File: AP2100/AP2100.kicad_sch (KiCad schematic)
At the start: 0 parts

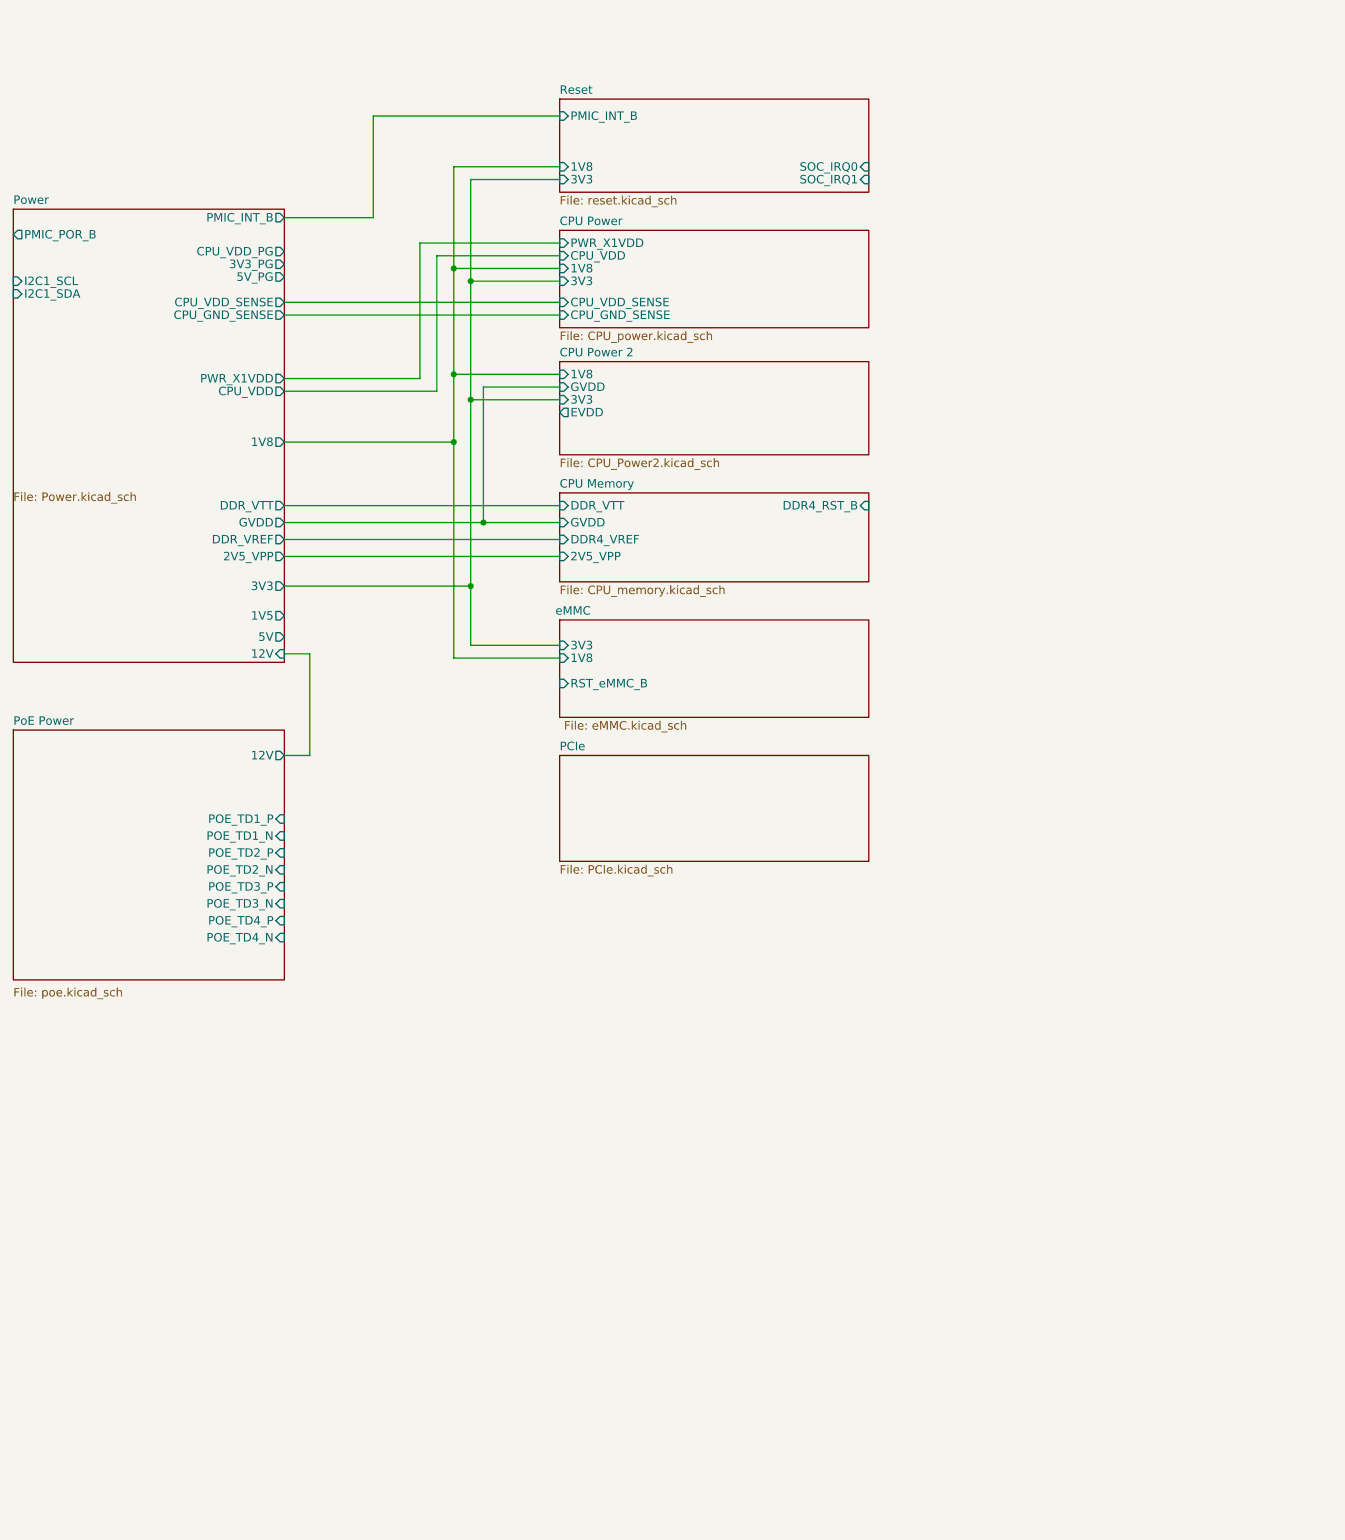
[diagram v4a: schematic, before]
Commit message: Add clocking and start of ethernet
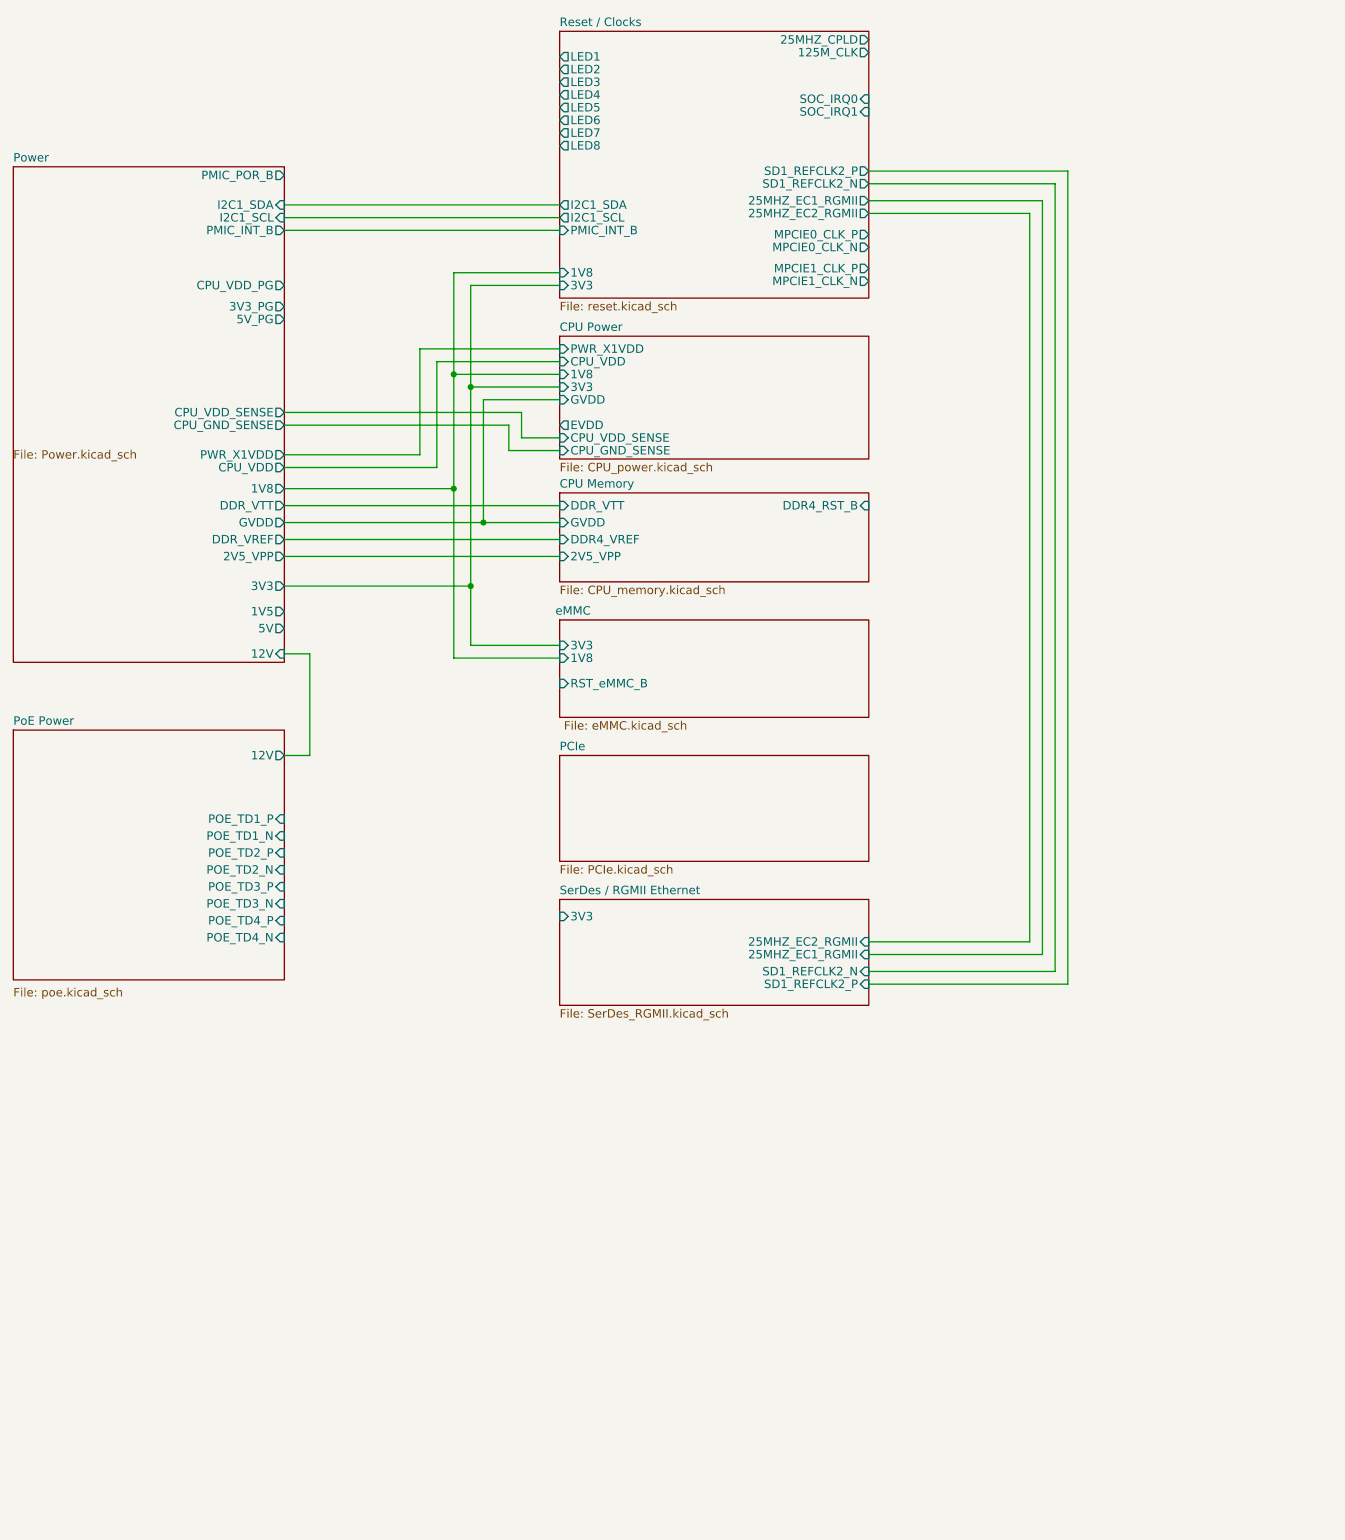
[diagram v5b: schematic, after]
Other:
- sheet Reset renamed Reset / Clocks
- removed sheet CPU Power 2
- added sheet SerDes / RGMII Ethernet (SerDes_RGMII.kicad_sch)
- sheet CPU Power ports: added EVDD, GVDD; removed none
- sheet Reset / Clocks ports: added 125M_CLK, 25MHZ_CPLD, 25MHZ_EC1_RGMII, 25MHZ_EC2_RGMII, I2C1_SCL, I2C1_SDA, LED1, LED2, LED3, LED4, LED5, LED6, LED7, LED8, MPCIE0_CLK_N, MPCIE0_CLK_P, MPCIE1_CLK_N, MPCIE1_CLK_P, SD1_REFCLK2_N, SD1_REFCLK2_P; removed none

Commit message: Finish reset section
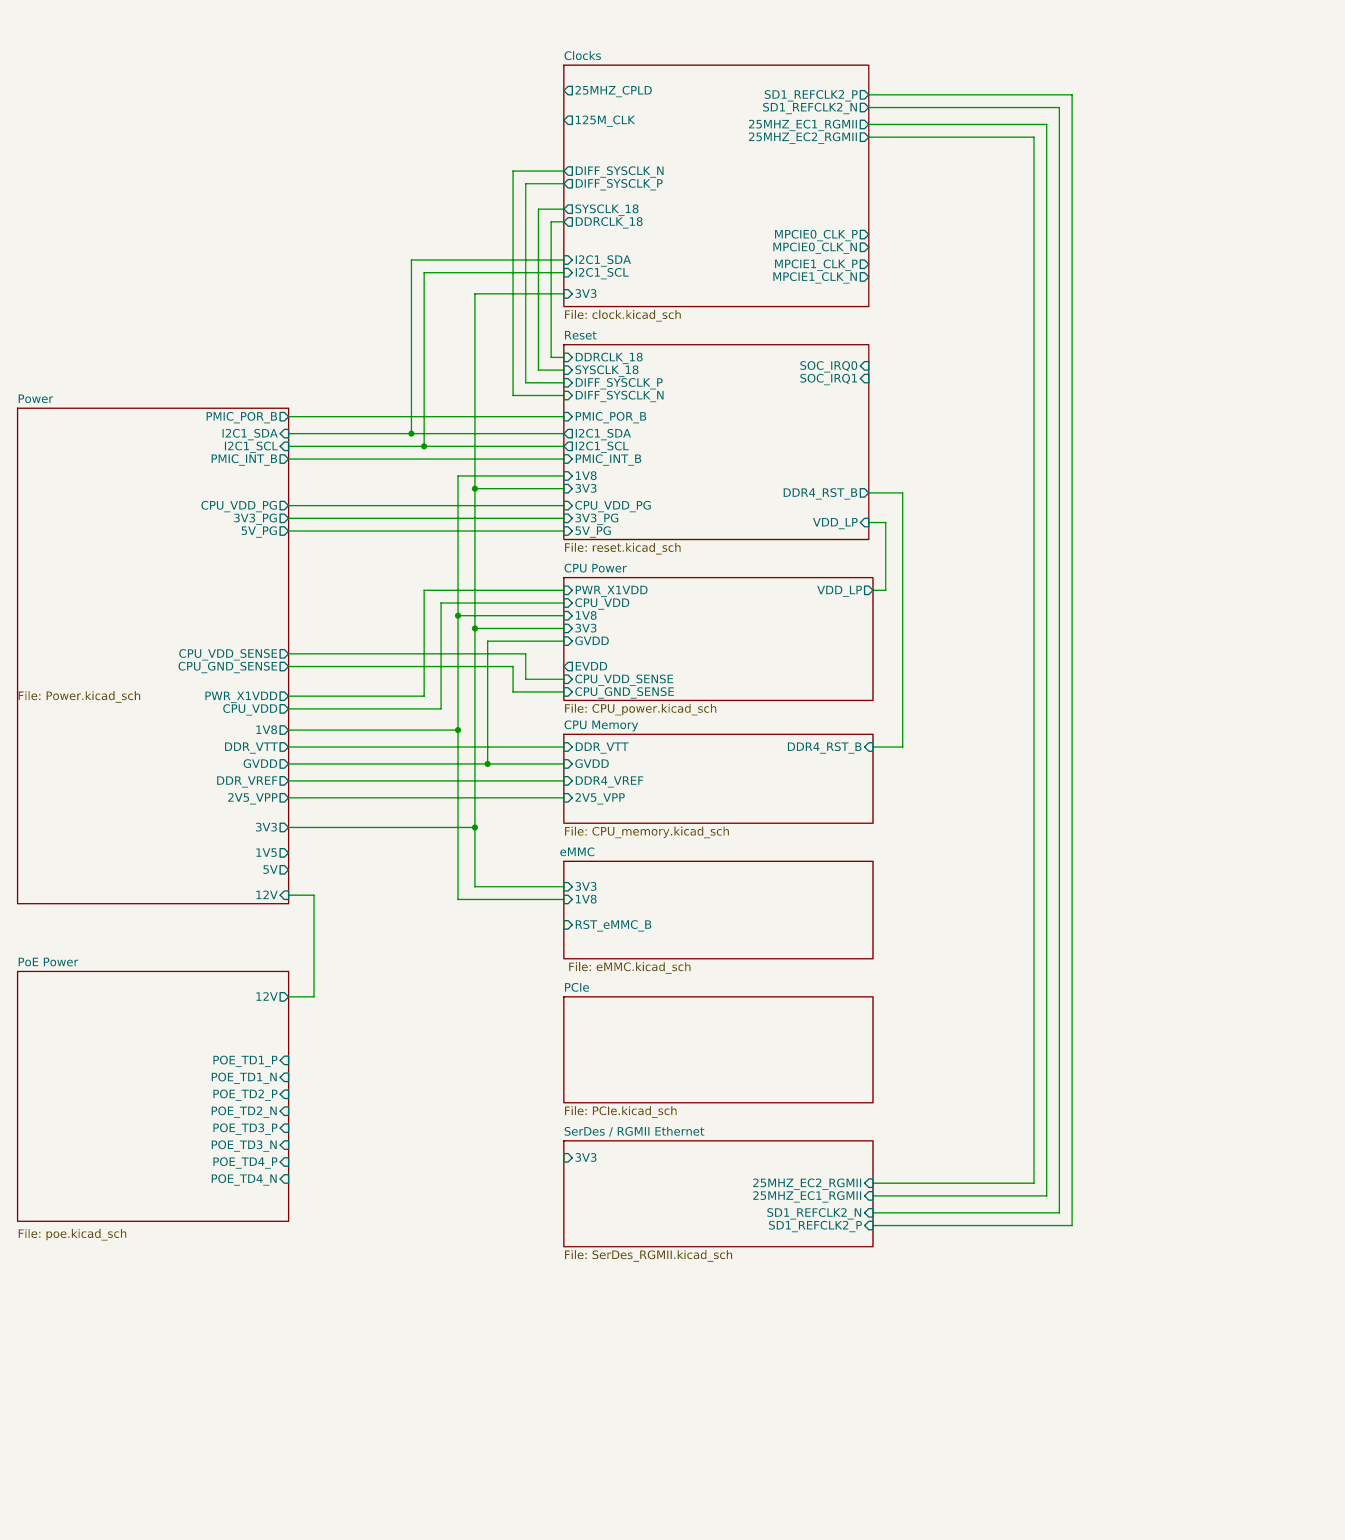
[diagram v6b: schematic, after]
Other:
- sheet Reset / Clocks renamed Reset
- added sheet Clocks (clock.kicad_sch)
- sheet CPU Power ports: added VDD_LP; removed none
- sheet Reset ports: added 3V3_PG, 5V_PG, CPU_VDD_PG, DDR4_RST_B, DDRCLK_18, DIFF_SYSCLK_N, DIFF_SYSCLK_P, PMIC_POR_B, SYSCLK_18, VDD_LP; removed 125M_CLK, 25MHZ_CPLD, 25MHZ_EC1_RGMII, 25MHZ_EC2_RGMII, LED1, LED2, LED3, LED4, LED5, LED6, LED7, LED8, MPCIE0_CLK_N, MPCIE0_CLK_P, MPCIE1_CLK_N, MPCIE1_CLK_P, SD1_REFCLK2_N, SD1_REFCLK2_P

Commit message: Mostly done with USB - USB1 complete just duplicate to 2+3
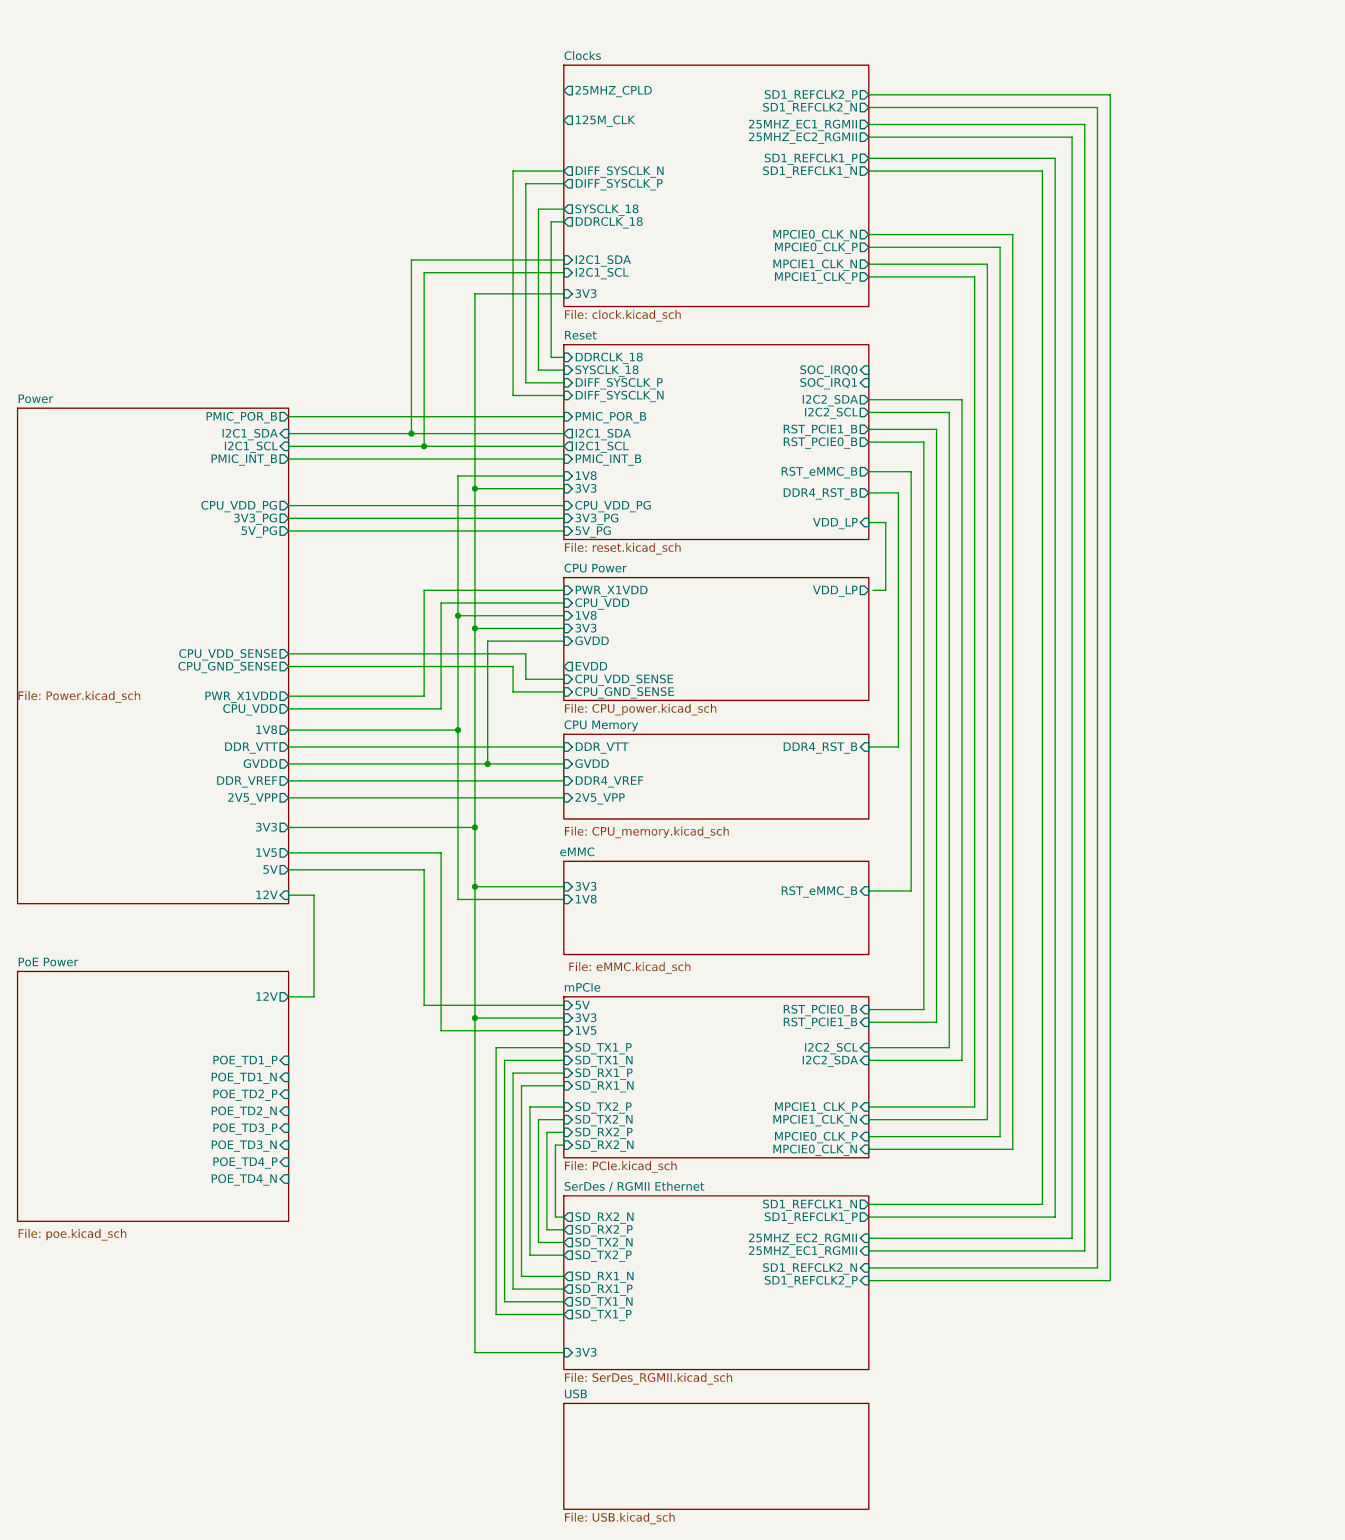
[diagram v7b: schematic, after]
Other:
- sheet PCIe renamed mPCIe
- added sheet USB (USB.kicad_sch)
- sheet Clocks ports: added SD1_REFCLK1_N, SD1_REFCLK1_P; removed none
- sheet Reset ports: added I2C2_SCL, I2C2_SDA, RST_PCIE0_B, RST_PCIE1_B, RST_eMMC_B; removed none
- sheet SerDes / RGMII Ethernet ports: added SD1_REFCLK1_N, SD1_REFCLK1_P, SD_RX1_N, SD_RX1_P, SD_RX2_N, SD_RX2_P, SD_TX1_N, SD_TX1_P, SD_TX2_N, SD_TX2_P; removed none
- sheet mPCIe ports: added 1V5, 3V3, 5V, I2C2_SCL, I2C2_SDA, MPCIE0_CLK_N, MPCIE0_CLK_P, MPCIE1_CLK_N, MPCIE1_CLK_P, RST_PCIE0_B, RST_PCIE1_B, SD_RX1_N, SD_RX1_P, SD_RX2_N, SD_RX2_P, SD_TX1_N, SD_TX1_P, SD_TX2_N, SD_TX2_P; removed none
